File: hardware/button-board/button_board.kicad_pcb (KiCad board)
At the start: 2 copper layers, 48.3 x 91.4 mm, 15 parts, among them J1 Conn_01x05_Pin, SW1 RotaryEncoder_Switch, SW2 SW_Push, SW3 SW_Push, SW4 SW_Push, SW5 SW_Push, U1 MCP23S17_SP

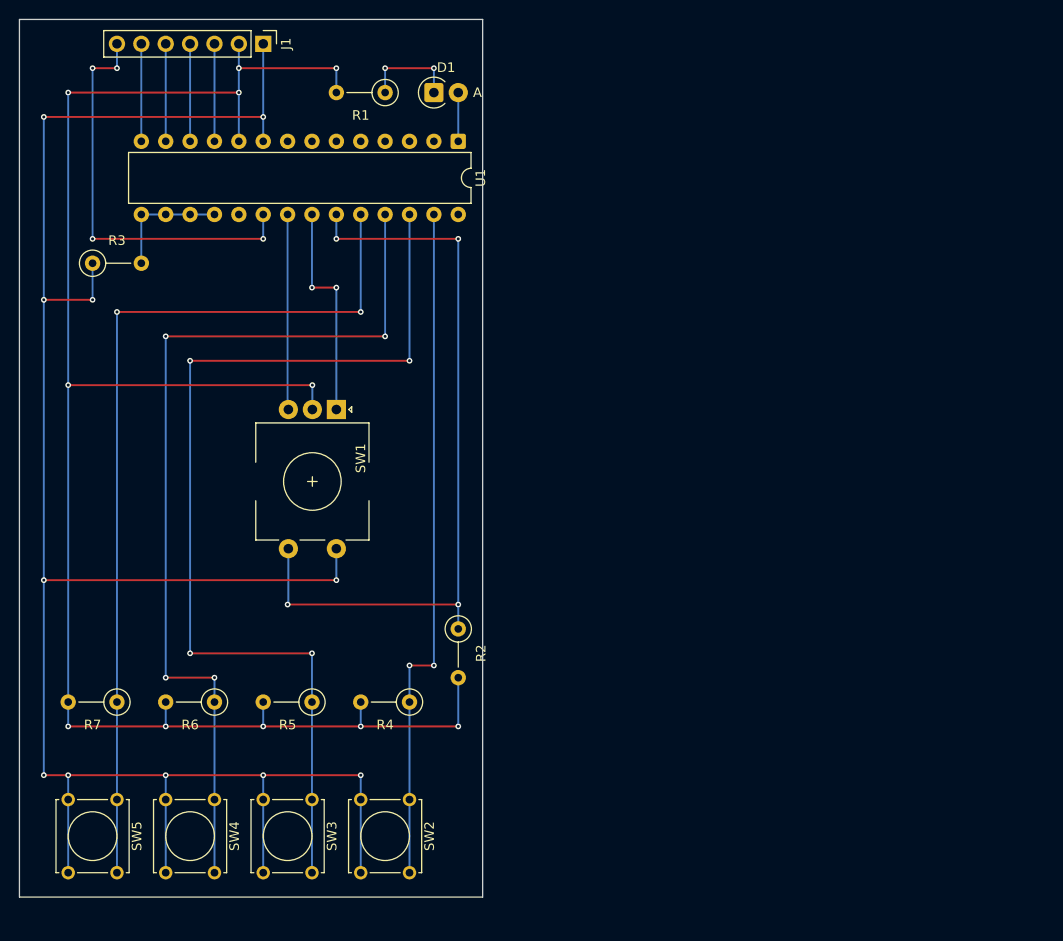
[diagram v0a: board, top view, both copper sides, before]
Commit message: Button board hardware design
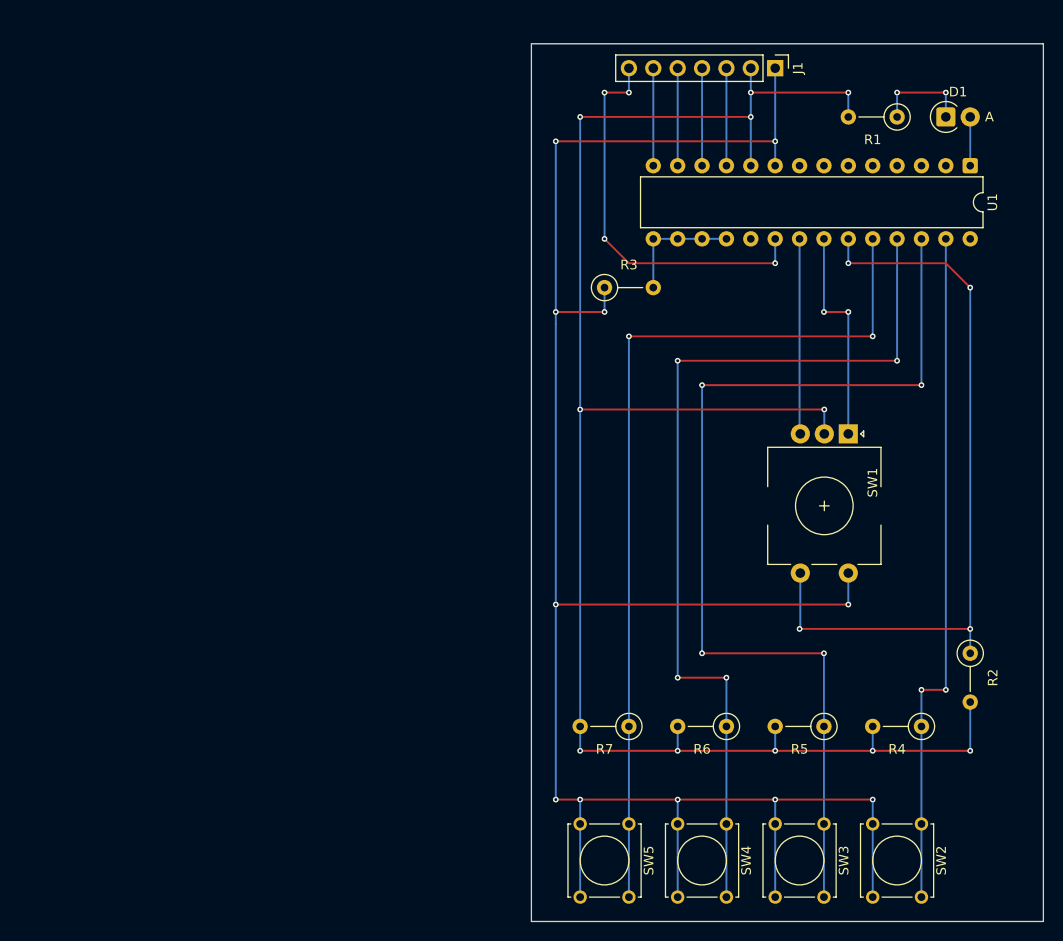
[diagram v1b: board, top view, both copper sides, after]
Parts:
- R1: value 1K -> 510
- moved R5 53.4 mm to (149.9, 111.8)
- moved SW3 53.4 mm to (149.9, 121.9)
- moved D1 53.4 mm to (162.6, 48.3)
- moved J1 53.4 mm to (144.8, 43.2)
- moved R3 53.4 mm to (127.0, 66.0)
- moved R4 53.4 mm to (160.0, 111.8)
- moved SW1 53.4 mm to (152.4, 81.3)
- moved SW2 53.4 mm to (160.0, 121.9)
- moved R1 53.4 mm to (157.5, 48.3)
- moved R2 53.4 mm to (165.1, 104.1)
- moved R6 53.4 mm to (139.7, 111.8)
- moved R7 53.4 mm to (129.5, 111.8)
- moved SW4 53.4 mm to (139.7, 121.9)
- moved SW5 53.4 mm to (129.5, 121.9)
- moved U1 53.4 mm to (165.1, 53.3)
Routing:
- net /ROT-SW: track 79.5 -> 78.0 mm
- net /INTA: track 43.2 -> 41.7 mm
- net +3.3V: track 217.9 -> 216.6 mm
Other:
- board size 48.3 x 91.4 mm -> 53.3 x 91.4 mm
- board text added: "01"
- board text added: "02"
- board text added: "03"
- board text added: "04"
- board text added: "05"
- board text added: "06"
- board text added: "07"
- board text added: "08"
- board text added: "09"
- board text added: "10"
- board text added: "11"
- board text added: "12"
- board text added: "13"
- board text added: "14"
- board text added: "15"
- board text added: "16"
- board text added: "17"
- board text added: "18"
- board text added: "19"
- board text added: "20"
- board text added: "21"
- board text added: "22"
- board text added: "23"
- board text added: "24"
- board text added: "25"
- board text added: "26"
- board text added: "27"
- board text added: "28"
- board text added: "29"
- board text added: "30"
- board text added: "31"
- board text added: "32"
- board text added: "33"
- board text added: "34"
- board text added: "35"
- board text added: "A"
- board text added: "B"
- board text added: "C"
- board text added: "D"
- board text added: "E"
- board text added: "F"
- board text added: "G"
- board text added: "H"
- board text added: "I"
- board text added: "J"
- board text added: "K"
- board text added: "L"
- board text added: "M"
- board text added: "N"
- board text added: "O"
- board text added: "P"
- board text added: "Q"
- board text added: "R"
- board text added: "S"
- board text added: "T"

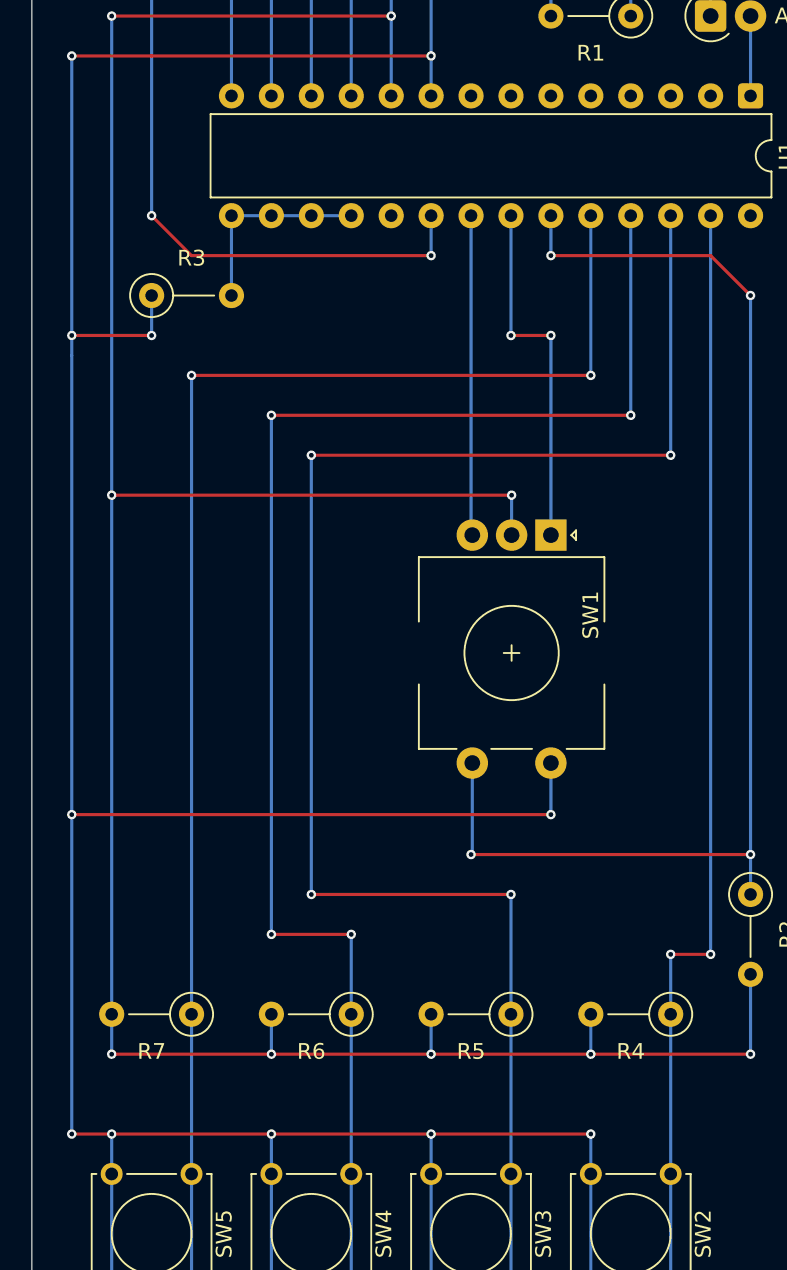
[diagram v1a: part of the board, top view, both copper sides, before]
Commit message: Preset buttons work (without interrupt logic)
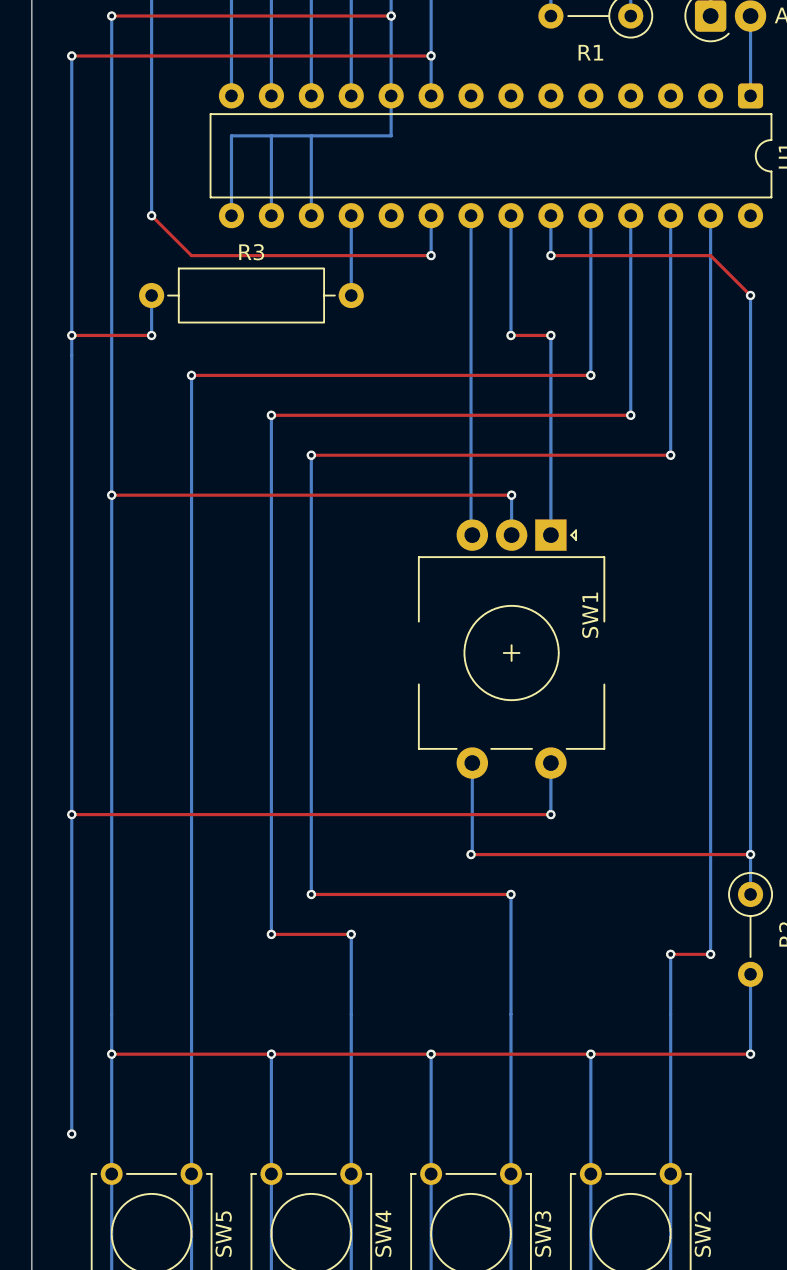
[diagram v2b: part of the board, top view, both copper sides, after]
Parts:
- removed R4, R5, R6, R7: 10K, Resistor_THT:R_Axial_DIN0207_L6.3mm_D2.5mm_P5.08mm_Vertical
- D1: value LED -> GREEN
- R3: footprint Resistor_THT:R_Axial_DIN0207_L6.3mm_D2.5mm_P5.08mm_Vertical -> Resistor_THT:R_Axial_DIN0309_L9.0mm_D3.2mm_P12.70mm_Horizontal
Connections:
- R3 pad 2: Net-(U1-A0) -> Net-(U1-~{RESET})
- SW2 pad 2: +3.3V -> GND
- SW3 pad 2: +3.3V -> GND
- SW4 pad 2: +3.3V -> GND
- SW5 pad 2: +3.3V -> GND
- U1 pad 15: Net-(U1-A0) -> GND
- U1 pad 16: Net-(U1-A0) -> GND
- U1 pad 17: Net-(U1-A0) -> GND
- U1 pad 18: Net-(U1-A0) -> Net-(U1-~{RESET})
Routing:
- net GND: track 188.0 -> 269.3 mm
- net +3.3V: track 216.6 -> 143.0 mm, vias 11 -> 7
- net Net-(U1-A0): track 12.7 -> 0.00 mm
- net Net-(U1-~{RESET}): track 0.00 -> 5.08 mm
